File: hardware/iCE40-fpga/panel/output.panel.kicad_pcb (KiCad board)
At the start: 4 copper layers, 50 x 22.9 mm, 140 parts, among them J1 USB_B_Micro, J2 JST_PH, J3 Feather, Q1 DMP2045U, U1 MCP73831-2-OT, U2 W25Q32JVZP, U3 AP2112K-3.3, U4 ICE40UP5K-SG48ITR, U5 NCV8114ASN120T1G, U6 93C46B, U7 FT2232H, X1 DSC6101CI1A

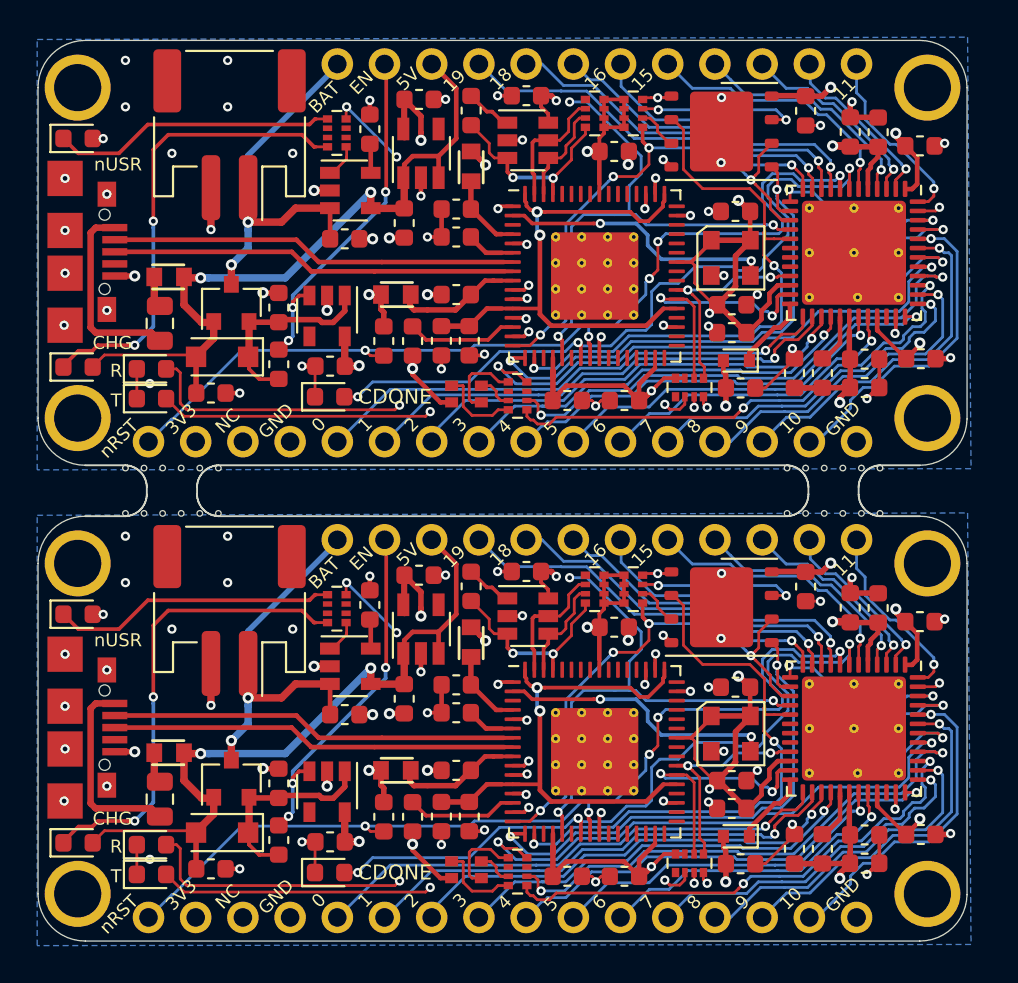
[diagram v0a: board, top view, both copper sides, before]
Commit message: moved battery connector and generated new gerbers for FPGA
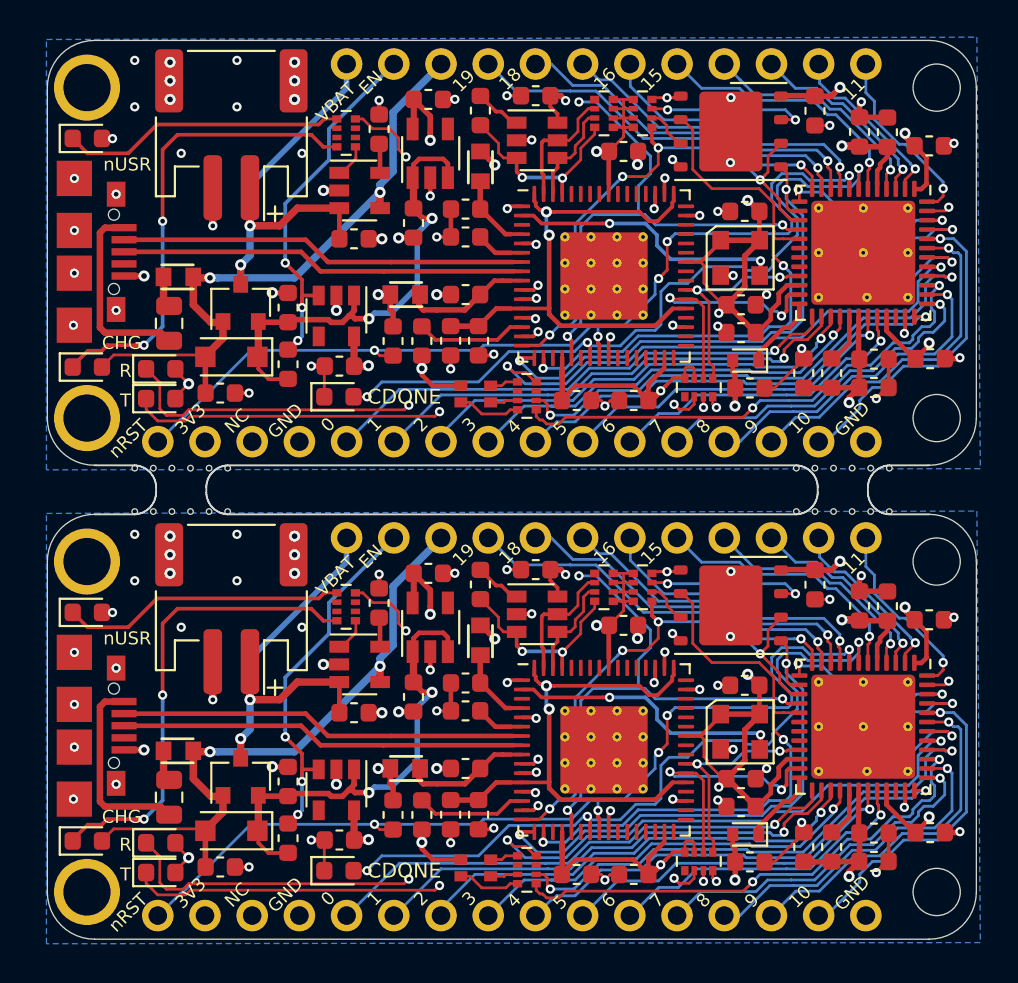
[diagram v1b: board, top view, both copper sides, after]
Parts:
- removed the ? at (71.6, 47.9)
- removed the ? at (66.6, 45.4)
- removed the ? at (36.0, 47.9)
- removed the ? at (31.0, 45.4)
- removed the J2 at (36.6, 53.1)
- removed the J2 at (36.6, 27.5)
- removed the J3 at (51.3, 59.5)
- removed the J3 at (51.3, 33.9)
- added ?: , holes, F.Cu at (72.1, 47.8)
- added ?: , holes, F.Cu at (67.1, 45.4)
- added ?: , holes, F.Cu at (31.5, 45.4)
- added ?: , holes, F.Cu at (36.5, 47.8)
- added G***: LOGO, josh-logos:josh-johnson-logo-8_6x1_5, B.Cu at (42.1, 61.3)
- added G***: LOGO, josh-logos:josh-johnson-logo-8_6x1_5, B.Cu at (42.1, 35.8)
- added J2: JST_PH, josh-connectors:JST_PH_S2B-PH-SM4-TB_1x02-1MP_P2.00mm_Horizontal, F.Cu at (36.7, 53.0)
- added J2: JST_PH, josh-connectors:JST_PH_S2B-PH-SM4-TB_1x02-1MP_P2.00mm_Horizontal, F.Cu at (36.7, 27.5)
- added J3: Feather, josh-connectors:featherwing, F.Cu at (51.8, 59.4)
- added J3: Feather, josh-connectors:featherwing, F.Cu at (51.8, 33.9)
- D7 (x2): value LED -> RED
- moved G*** 5.36 mm to (30.3, 61.2)
- moved G*** 5.31 mm to (30.3, 35.7)
- moved REF** 4.36 mm to (41.5, 62.9)
- moved REF** 4.30 mm to (41.5, 37.4)
- moved C11 0.51 mm to (74.3, 65.0)
- moved C18 0.51 mm to (71.3, 66.6)
- moved C35 0.51 mm to (55.3, 67.3)
- moved C36 0.51 mm to (58.4, 67.3)
- moved D5 0.51 mm to (42.5, 67.1)
- moved D8 0.51 mm to (32.9, 65.6)
- moved R14 0.51 mm to (47.0, 64.1)
- moved R4 0.51 mm to (39.8, 65.3)
- moved R5 0.51 mm to (45.4, 64.1)
- moved RN3 0.51 mm to (52.6, 67.0)
- moved RN4 0.51 mm to (61.9, 66.6)
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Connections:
- net /ICE_SCK renamed /FLASH_SCK
- net /ICE_SS renamed /FLASH_SS
- net /IO0 renamed /IO_0
- net /IO1 renamed /IO_1
- net /IO10 renamed /IO_10
- net /IO11 renamed /IO_11
- net /IO12 renamed /IO_12
- net /IO13 renamed /IO_13
- net /IO14 renamed /IO_14
- net /IO15 renamed /IO_15
- net /IO16 renamed /IO_16
- net /IO17 renamed /IO_17
- net /IO18 renamed /IO_18
- net /IO19 renamed /IO_19
- net /IO2 renamed /IO_2
- net /IO3 renamed /IO_3
- net /IO4 renamed /IO_4
- net /IO5 renamed /IO_5
- net /IO6 renamed /IO_6
- net /IO7 renamed /IO_7
- net /IO8 renamed /IO_8
- net /IO9 renamed /IO_9
- net /RX_FPGA renamed /UART_RX
- net /TX_FPGA renamed /UART_TX
- net /nLED_BLUE renamed /nLED_BLU
- net /nLED_GREEN renamed /nLED_GRN
- C5 pad 1: +5V -> Net-(C1-Pad1) (x2)
- D3 pad 1: GND -> Net-(D3-Pad1) (x2)
- D3 pad 2: Net-(D3-Pad2) -> +3V3 (x2)
- D8 pad 1: GND -> Net-(D8-Pad1) (x2)
- D8 pad 2: Net-(D8-Pad2) -> +3V3 (x2)
- J1 pad 4: (no net) -> Net-(J1-Pad4) (x2)
- RN2 pad 1: (no net) -> Net-(RN2-Pad1) (x2)
- RN3 pad 3: (no net) -> Net-(RN3-Pad3) (x2)
- RN3 pad 6: (no net) -> Net-(RN3-Pad6) (x2)
- RN4 pad 1: (no net) -> Net-(RN4-Pad1) (x2)
- RN4 pad 3: Net-(D8-Pad2) -> Net-(D8-Pad1) (x2)
- RN4 pad 4: Net-(D3-Pad2) -> Net-(D3-Pad1) (x2)
- RN5 pad 2: (no net) -> Net-(RN5-Pad2) (x2)
- RN5 pad 3: (no net) -> Net-(RN5-Pad3) (x2)
- RN5 pad 6: (no net) -> Net-(RN5-Pad6) (x2)
- RN5 pad 7: (no net) -> Net-(RN5-Pad7) (x2)
- U3 pad 4: (no net) -> Net-(U3-Pad4) (x2)
- U4 pad 18: (no net) -> Net-(U4-Pad18) (x2)
- U4 pad 19: (no net) -> Net-(U4-Pad19) (x2)
- U4 pad 20: (no net) -> Net-(U4-Pad20) (x2)
- U4 pad 34: (no net) -> Net-(U4-Pad34) (x2)
- U5 pad 1: +5V -> Net-(C1-Pad1) (x2)
- U5 pad 3: +5V -> Net-(C1-Pad1) (x2)
- U5 pad 4: (no net) -> Net-(U5-Pad4) (x2)
- U7 pad 19: (no net) -> Net-(U7-Pad19) (x2)
- U7 pad 22: (no net) -> Net-(U7-Pad22) (x2)
- U7 pad 26: (no net) -> Net-(U7-Pad26) (x2)
- U7 pad 27: (no net) -> Net-(U7-Pad27) (x2)
- U7 pad 28: (no net) -> Net-(U7-Pad28) (x2)
- U7 pad 29: (no net) -> Net-(U7-Pad29) (x2)
- U7 pad 3: (no net) -> Net-(U7-Pad3) (x2)
- U7 pad 30: (no net) -> Net-(U7-Pad30) (x2)
- U7 pad 32: (no net) -> Net-(U7-Pad32) (x2)
- U7 pad 33: (no net) -> Net-(U7-Pad33) (x2)
- U7 pad 34: (no net) -> Net-(U7-Pad34) (x2)
- U7 pad 36: (no net) -> Net-(U7-Pad36) (x2)
- U7 pad 40: (no net) -> Net-(U7-Pad40) (x2)
- U7 pad 41: (no net) -> Net-(U7-Pad41) (x2)
- U7 pad 43: (no net) -> Net-(U7-Pad43) (x2)
- U7 pad 44: (no net) -> Net-(U7-Pad44) (x2)
- U7 pad 45: (no net) -> Net-(U7-Pad45) (x2)
- U7 pad 46: (no net) -> Net-(U7-Pad46) (x2)
- U7 pad 48: (no net) -> Net-(U7-Pad48) (x2)
- U7 pad 52: (no net) -> Net-(U7-Pad52) (x2)
- U7 pad 53: (no net) -> Net-(U7-Pad53) (x2)
- U7 pad 54: (no net) -> Net-(U7-Pad54) (x2)
- U7 pad 55: (no net) -> Net-(U7-Pad55) (x2)
- U7 pad 57: (no net) -> Net-(U7-Pad57) (x2)
- U7 pad 58: (no net) -> Net-(U7-Pad58) (x2)
- U7 pad 59: (no net) -> Net-(U7-Pad59) (x2)
- U7 pad 60: (no net) -> Net-(U7-Pad60) (x2)
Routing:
- net Net-(D8-Pad1): track 0.00 -> 67.2 mm, vias 0 -> 4
- net Net-(D3-Pad1): track 0.00 -> 67.0 mm, vias 0 -> 4
- net Net-(D8-Pad2): track 63.8 -> 0.00 mm, vias 4 -> 0
- net Net-(D3-Pad2): track 62.7 -> 0.00 mm, vias 4 -> 0
- net Net-(C1-Pad1): track 21.8 -> 50.9 mm, vias 0 -> 4
- net +5V: track 78.5 -> 69.2 mm
- net GND: track 97.6 -> 89.0 mm, vias 112 -> 110
- net +3V3: track 147.3 -> 155.3 mm, vias 30 -> 32
- net Net-(D6-Pad1): track 8.62 -> 3.07 mm
- net Net-(D6-Pad3): track 8.96 -> 6.80 mm
- net /LDO_EN: track 38.4 -> 40.4 mm
- net /nLED: track 79.3 -> 78.0 mm, vias 6 -> 4
- net Net-(D6-Pad2): track 3.86 -> 2.98 mm
- net +BATT: track 45.5 -> 46.0 mm
- net (no net): vias 0 -> 12
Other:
- board size 50 x 22.9 mm -> 44.9 x 48.4 mm
- board text added: "12"
- board text added: "13"
- board text added: "14"
- board text added: "17"
- board text added: "VBAT"
- board text added: "VUSB"
- board text removed: "5V"
- board text removed: "BAT"
